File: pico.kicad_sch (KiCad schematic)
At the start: 90 parts, among them J101 Programming, J102 ???, J103 XT60, J104 MR30, J105 MR30, Q101 IRFS7434TRL7PP, Q102 SQJ142EP-T1_GE3, Q103 SQJ142EP-T1_GE3, Q104 SQJ142EP-T1_GE3, Q105 SQJ142EP-T1_GE3, Q106 SQJ142EP-T1_GE3, Q107 SQJ142EP-T1_GE3, Q108 SQJ142EP-T1_GE3, Q109 SQJ142EP-T1_GE3, Q110 SQJ142EP-T1_GE3, Q111 SQJ142EP-T1_GE3, Q112 SQJ142EP-T1_GE3, Q113 SQJ142EP-T1_GE3, U101 TPS7A2050PDBVR, U104 DRV8323SRTAT, U105 DRV8323SRTAT, U106 ADC124S051CIMM/NOPB

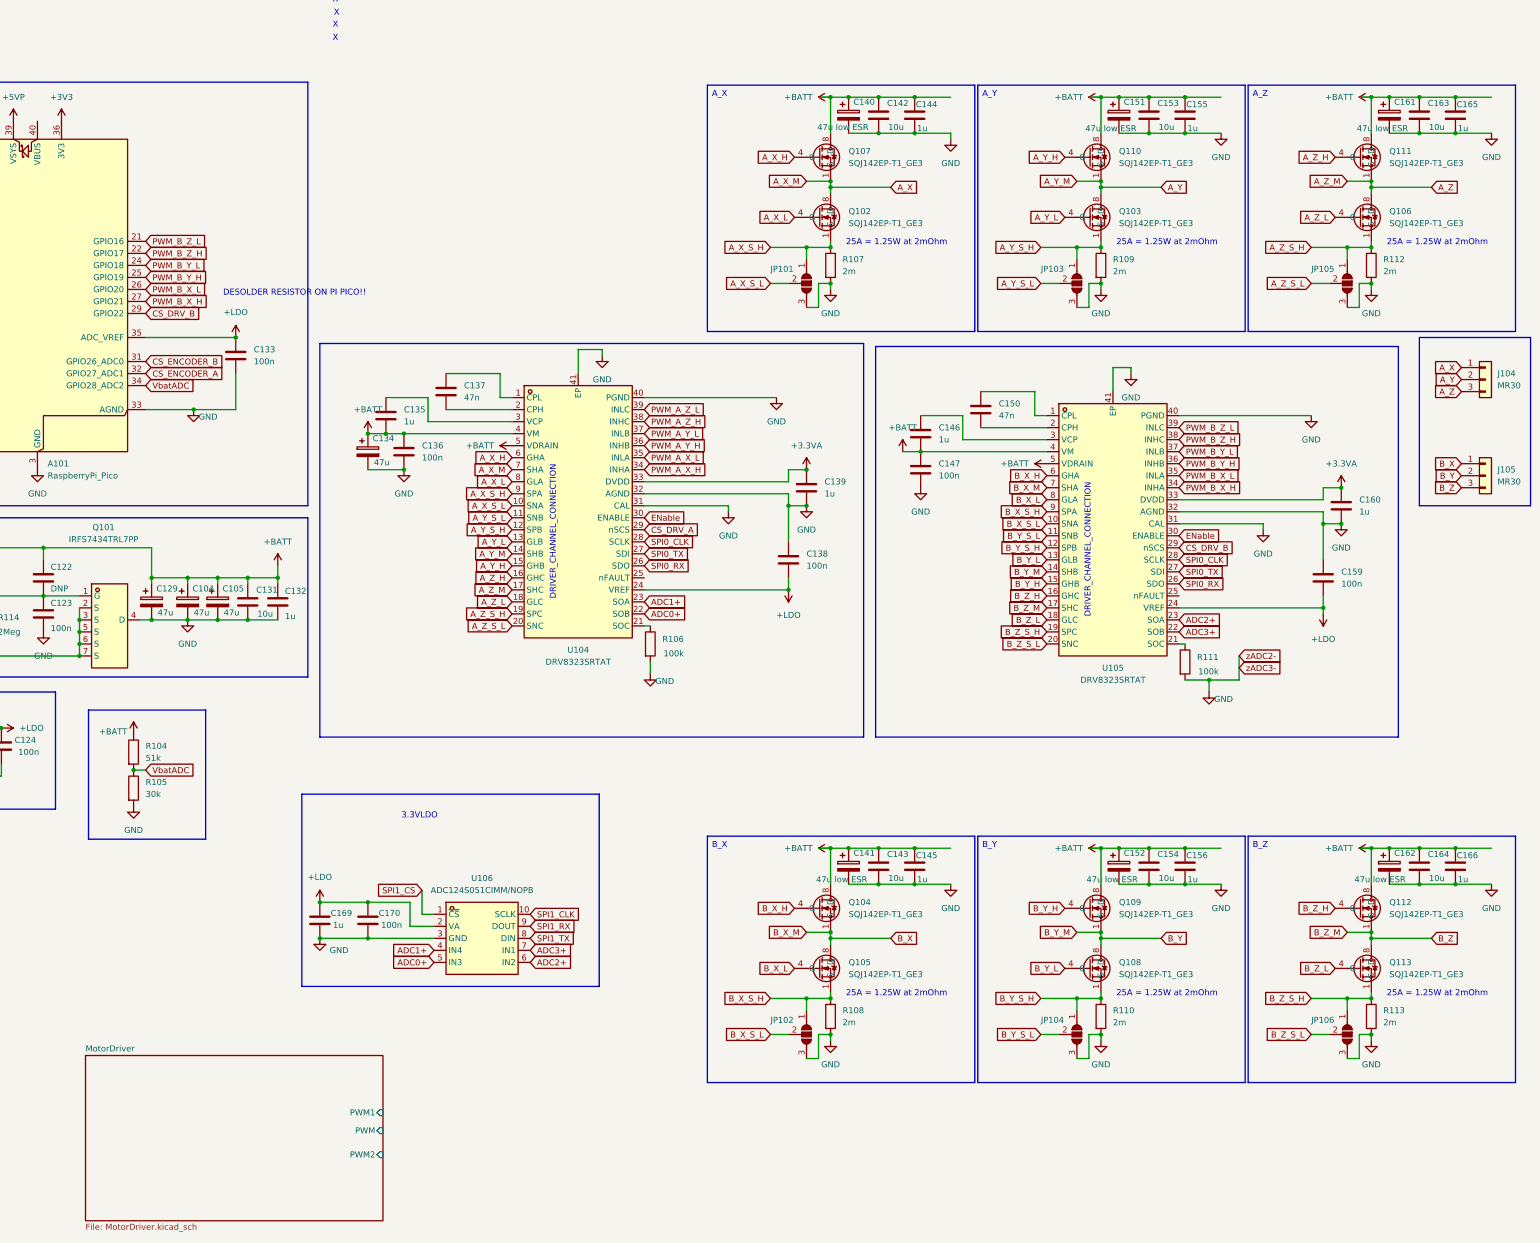
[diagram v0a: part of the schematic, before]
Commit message: seprate motors
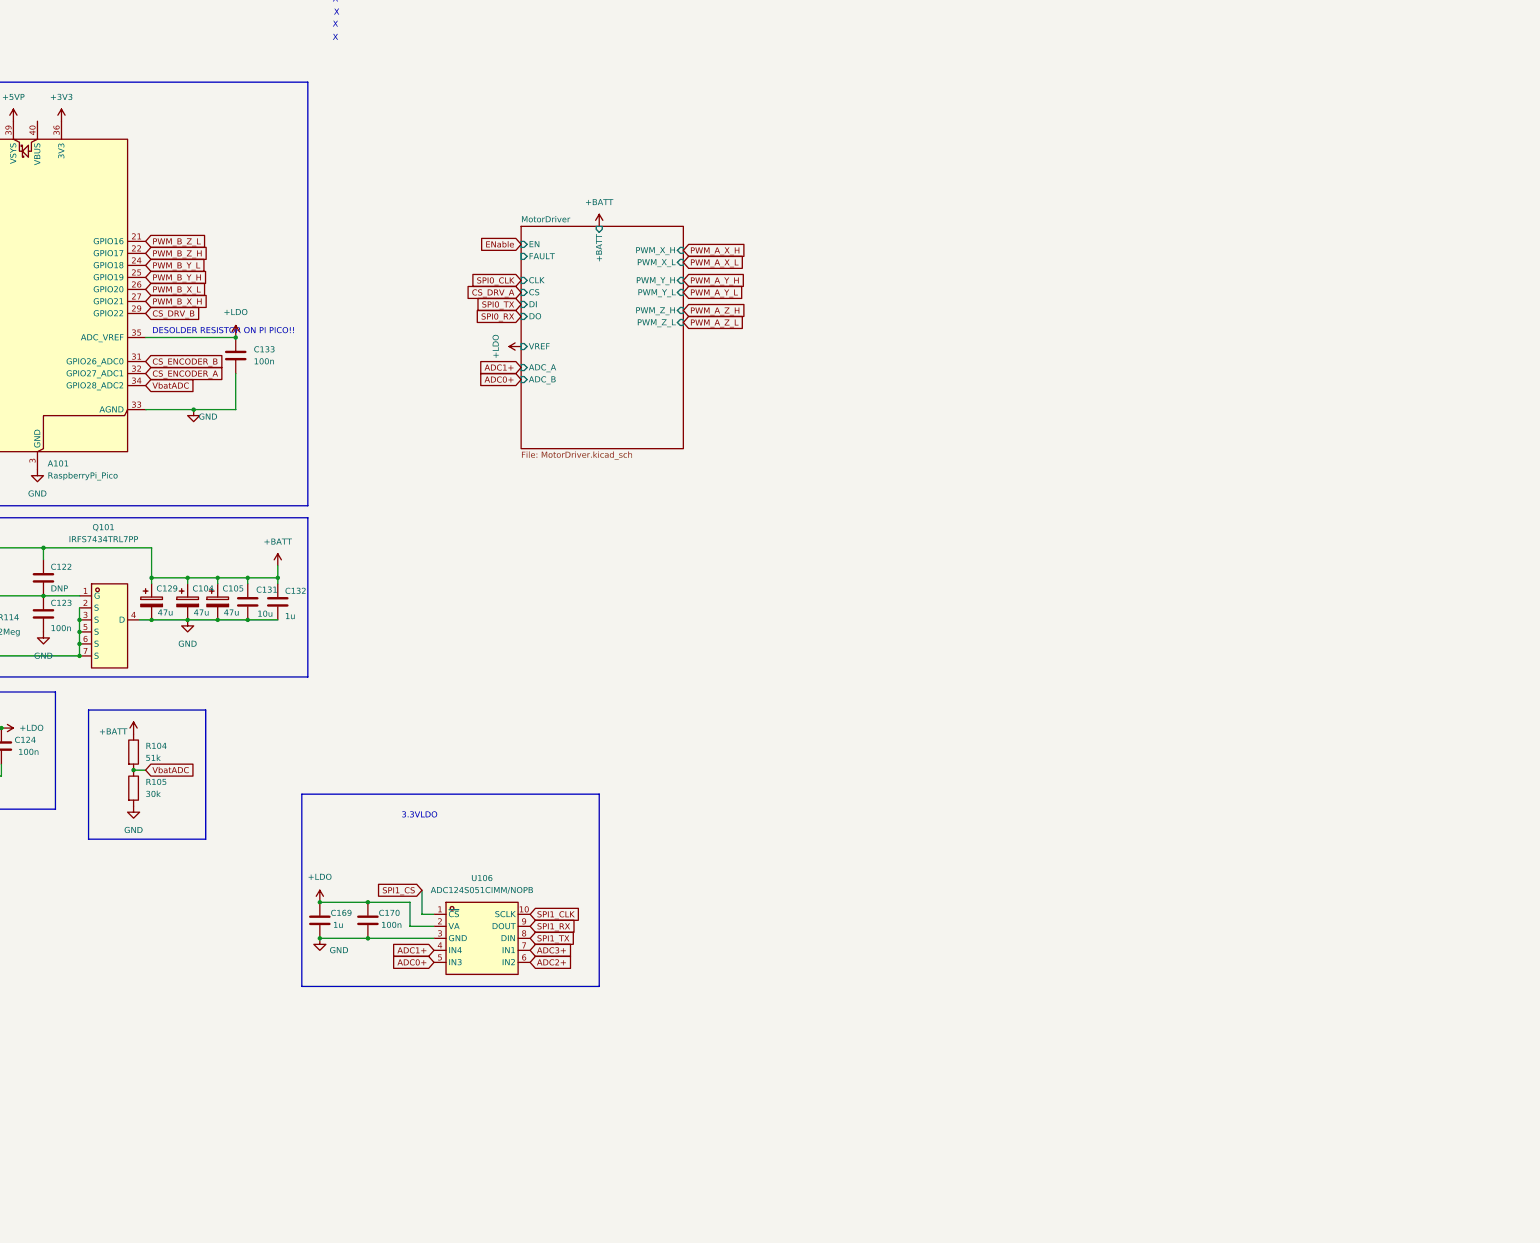
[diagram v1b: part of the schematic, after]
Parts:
- removed C134: 47u, Capacitor_THT:CP_Radial_D6.3mm_P2.50mm, symbol Device:C_Polarized
- removed C135, C139, C144, C145, C146, C155, C156, C160, C165, C166: 1u, COMPONENTS:1206_Resistor, symbol Device:C
- removed C136, C138, C147, C159: 100n, COMPONENTS:1206_Resistor, symbol Device:C
- removed C137, C150: 47n, COMPONENTS:1206_Resistor, symbol Device:C
- removed C140, C141, C151, C152, C161, C162: 47u low ESR, Capacitor_THT:CP_Radial_D6.3mm_P2.50mm, symbol Device:C_Polarized
- removed C142, C143, C153, C154, C163, C164: 10u, COMPONENTS:1206_Resistor, symbol Device:C
- removed J104, J105: MR30, Connector_AMASS:AMASS_MR30PW-FB_1x03_P3.50mm_Horizontal, symbol Connector_Generic:Conn_01x03
- removed JP101, JP102, JP103, JP104, JP105, JP106: SolderJumper_3_Open, Jumper:SolderJumper-3_P1.3mm_Open_RoundedPad1.0x1.5mm_NumberLabels, symbol Jumper:SolderJumper_3_Open
- removed Q102, Q103, Q104, Q105, Q106, Q107, Q108, Q109, Q110, Q111, Q112, Q113: SQJ142EP-T1_GE3, JLCPCB_Transistors_Thyristors:POWERPAK-SO-8_L5.9-W4.9-P1.27-BL, symbol JLCPCB_Transistors_Thyristors:SQJ142EP-T1_GE3
- removed R106, R111: 100k, COMPONENTS:1206_Resistor, symbol Device:R
- removed R107, R108, R109, R110, R112, R113: 2m, COMPONENTS:1206_Resistor, symbol Device:R
- removed U104, U105: DRV8323SRTAT, JLCPCB_Power_Supply_Chip:WQFN-40_L6.0-W6.0-P0.50-TL-EP4.5, symbol JLCPCB_Power_Supply_Chip:DRV8323SRTAT
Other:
- sheet MotorDriver ports: added +BATT, ADC_A, ADC_B, CLK, CS, DI, DO, EN, FAULT, PWM_X_H, PWM_X_L, PWM_Y_H, PWM_Y_L, PWM_Z_H, PWM_Z_L, VREF; removed PWM, PWM1, PWM2
- note removed: "25A = 1.25W at 2mOhm"
- note removed: "DRIVER_CHANNEL_CONNECTION"

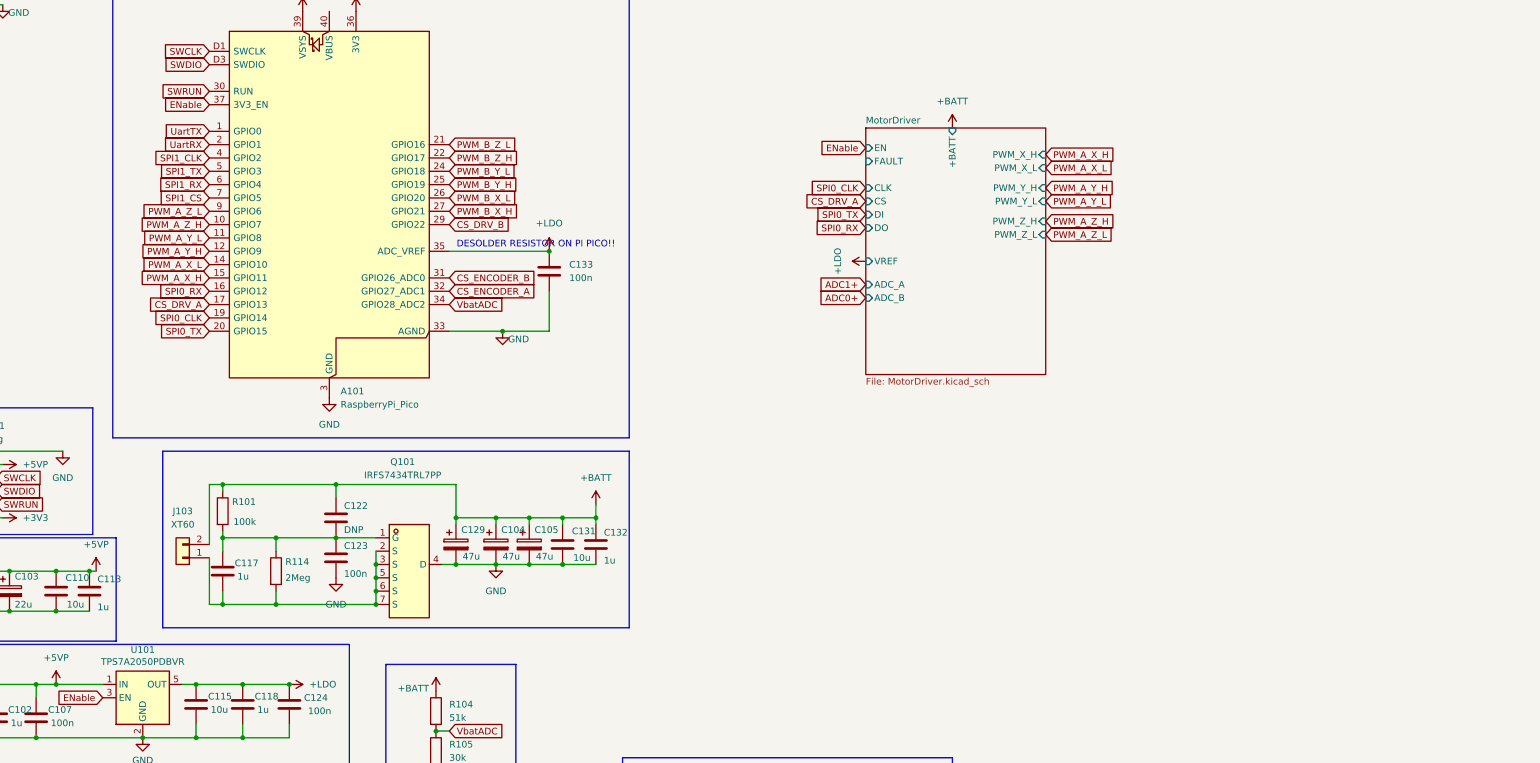
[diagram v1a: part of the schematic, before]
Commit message: progress on pcb todo:encoders
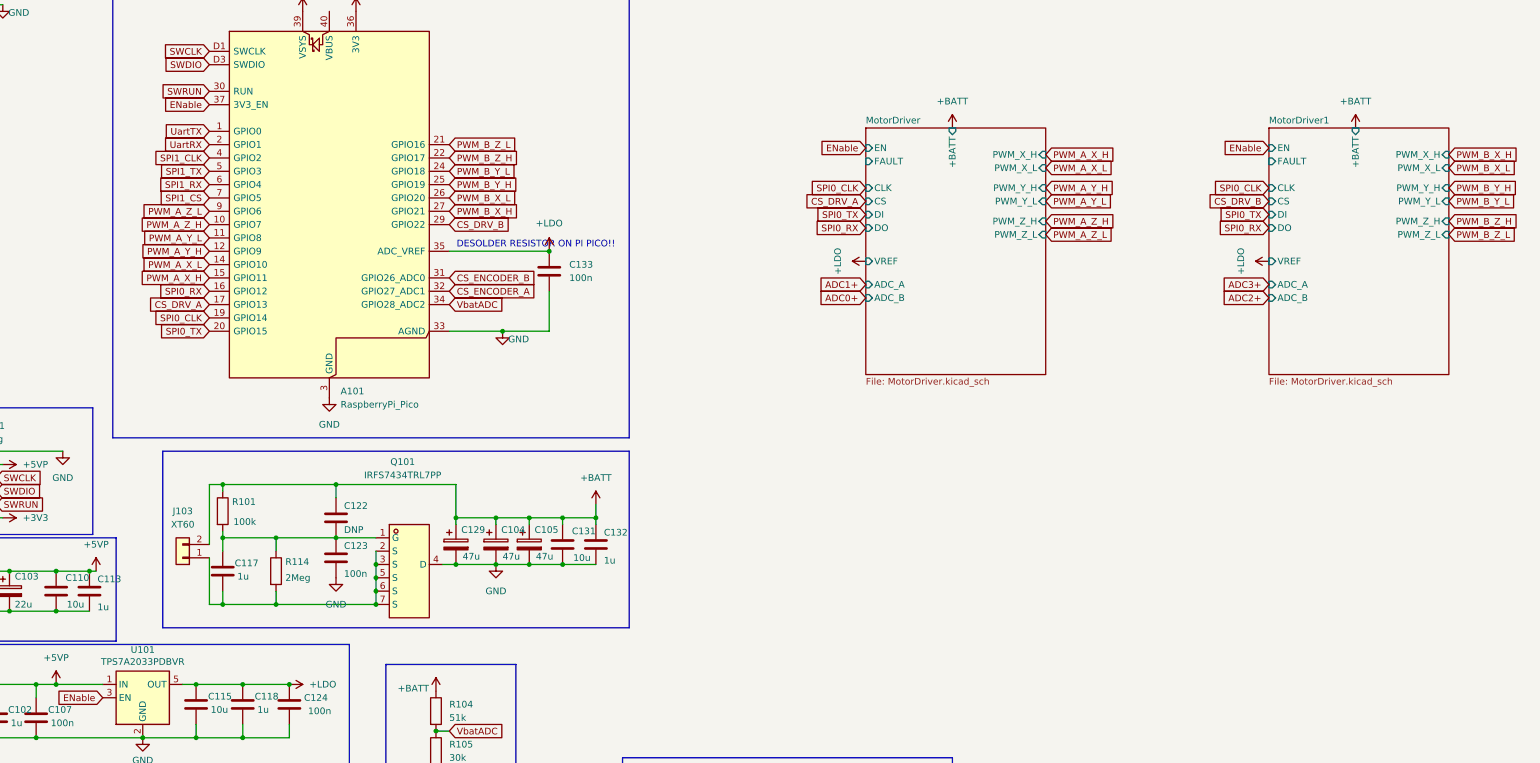
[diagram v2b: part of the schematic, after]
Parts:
- U101: value TPS7A2050PDBVR -> TPS7A2033PDBVR
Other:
- added sheet MotorDriver1 (MotorDriver.kicad_sch)

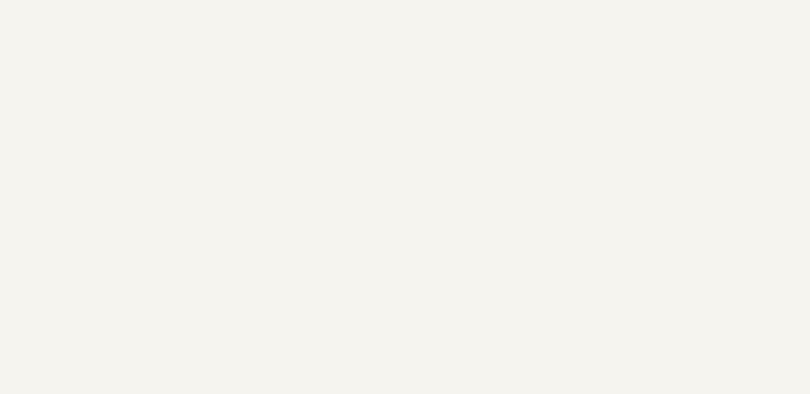
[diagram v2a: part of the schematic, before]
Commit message: added m3 mounting holes
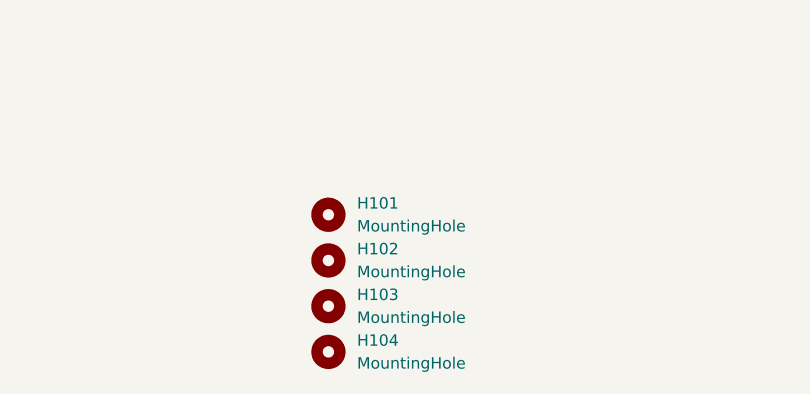
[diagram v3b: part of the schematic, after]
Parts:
- added H101, H102, H103, H104: MountingHole, MountingHole:MountingHole_3.2mm_M3, symbol Mechanical:MountingHole

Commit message: ewdwad
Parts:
- added J104: Conn_01x03, Connector_JST:JST_EH_B3B-EH-A_1x03_P2.50mm_Vertical, symbol Connector_Generic:Conn_01x03
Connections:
- net ENable: now also J104.1 (Pin_1)
- net UartRX: now also J104.2 (Pin_2)
- net UartTX: now also J104.3 (Pin_3)
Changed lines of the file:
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@@
 		)
 	)
+	(global_label "UartRX"
+		(shape input)
+		(at 31.75 66.04 0)
+		(fields_autoplaced yes)
+		(effects
+			(font
+				(size 1.27 1.27)
+			)
+			(justify left)
+		)
+		(property "Intersheetrefs" "${INTERSHEET_REFS}"
+			(at 41.2061 66.04 0)
+			(effects
+				(font
+					(size 1.27 1.27)
+				)
+				(justify left)
+				(hide yes)
+			)
+		)
+	)
 	(global_label "ADC1+"
 		(shape input)
@@
 		)
 	)
+	(global_label "ENable"
+		(shape input)
+		(at 31.75 68.58 0)
+		(fields_autoplaced yes)
+		(effects
+			(font
+				(size 1.27 1.27)
+			)
+			(justify left)
+		)
+		(property "Intersheetrefs" "${INTERSHEET_REFS}"
+			(at 41.2665 68.58 0)
+			(effects
+				(font
+					(size 1.27 1.27)
+				)
+				(justify left)
+				(hide yes)
+			)
+		)
+	)
+	(global_label "UartTX"
+		(shape input)
+		(at 31.75 63.5 0)
+		(fields_autoplaced yes)
+		(effects
+			(font
+				(size 1.27 1.27)
+			)
+			(justify left)
+		)
+		(property "Intersheetrefs" "${INTERSHEET_REFS}"
+			(at 40.9037 63.5 0)
+			(effects
+				(font
+					(size 1.27 1.27)
+				)
+				(justify left)
+				(hide yes)
+			)
+		)
+	)
 	(global_label "SPI1_CS"
 		(shape input)
@@
 					(unit 1)
 				)
+			)
+		)
+	)
+	(symbol
+		(lib_id "Connector_Generic:Conn_01x03")
+		(at 26.67 66.04 180)
+		(unit 1)
+		(exclude_from_sim no)
+		(in_bom yes)
+		(on_board yes)
+		(dnp no)
+		(fields_autoplaced yes)
+		(property "Reference" "J104"
+			(at 26.67 57.15 0)
+			(effects
+				(font
+					(size 1.27 1.27)
+				)
+			)
+		)
+		(property "Value" "Conn_01x03"
+			(at 26.67 59.69 0)
+			(effects
+				(font
+					(size 1.27 1.27)
+				)
+			)
+		)
+		(property "Footprint" "Connector_JST:JST_EH_B3B-EH-A_1x03_P2.50mm_Vertical"
+			(at 26.67 66.04 0)
+			(effects
+				(font
+					(size 1.27 1.27)
+				)
+				(hide yes)
+			)
+		)
+		(property "Datasheet" "~"
+			(at 26.67 66.04 0)
+			(effects
+				(font
+					(size 1.27 1.27)
+				)
+				(hide yes)
+			)
+		)
+		(property "Description" "Generic connector, single row, 01x03, script generated (kicad-library-utils/schlib/autogen/connector/)"
+			(at 26.67 66.04 0)
+			(effects
+				(font
+					(size 1.27 1.27)
+				)
+				(hide yes)
+			)
+		)
+		(pin "1"
+		)
+		(pin "3"
+		)
+		(pin "2"
+		)
+		(instances
+			(project ""
+				(path "/ee499c9f-2c44-4eb0-b36d-4920617b3177"
+					(reference "J104")
+					(unit 1)
+				)

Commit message: wdawdawd
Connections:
- net ADC2+: now also U106.7 (IN1); no longer U106.6 (IN2)
- net ADC3+: now also U106.6 (IN2); no longer U106.7 (IN1)

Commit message: why every commit needs a message
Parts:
- added Q102: BSS138, Package_TO_SOT_SMD:SOT-23, symbol Transistor_FET:BSS138
- added R102: 100, COMPONENTS:1206_Resistor, symbol Device:R
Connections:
- net +BATT: now also Q102.3 (D)
- net GND: now also R102.2
- net at C117.1, C122.2, C123.1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: now also Q102.2 (S)
- net at C117.2, J103.1 (Pin_1), Q101.2 (S)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: now also R102.1
- new net ENableBATT: Q102.1 (G)
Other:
- note added: "WILL SPLIT GND WORK??"
- moved on the sheet: C101, C102, C107, C115, C118, C124, R104, R105, U101

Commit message: Good progress
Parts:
- removed C117: 1u, COMPONENTS:1206_Resistor, symbol Device:C
- removed C122: DNP, COMPONENTS:1206_Resistor, symbol Device:C
- removed C123: 100n, COMPONENTS:1206_Resistor, symbol Device:C
- removed Q101: IRFS7434TRL7PP, JLCPCB_Transistors:D2PAK-7_L10.6-W9.6-P1.27-LS15.9-BR, symbol JLCPCB_Transistors:IRFS7434TRL7PP
- removed R114: 2Meg, COMPONENTS:1206_Resistor, symbol Device:R
- added C106: 2200u, Capacitor_THT:CP_Radial_D18.0mm_P7.50mm, symbol Device:C_Polarized
- added Q101, Q103, Q104, Q105, Q106: AGM30P100D, EasyEDA_Lib:TO-252-3_L6.6-W6.1-P4.57-LS9.9-BR-CW, symbol EasyEDA_Lib:AGM30P100D
- added R103, R106, R107: 100, COMPONENTS:1206_Resistor, symbol Device:R
- added R108: 5k, COMPONENTS:1206_Resistor, symbol Device:R
- R101: value 100k -> 100
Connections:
- net ENableBATT is gone; now on net ENable: Q102.1 (G)
- net +BATT: now also R101.2, R102.2, C106.1, Q101.2 (D), Q103.2 (D), Q104.2 (D), Q105.2 (D), Q106.2 (D), R103.2, R106.2, R107.2; no longer J103.2 (Pin_2), Q102.3 (D), R101.1
- net GND: now also J103.1 (Pin_1), Q102.2 (S), C106.2; no longer R102.2
- net IN: now reaches R102.1
- net IN: now also J103.2 (Pin_2), R101.1, Q101.3 (S), Q103.3 (S), Q104.3 (S), Q105.3 (S), Q106.3 (S), R103.1, R106.1, R107.1, R108.1; no longer J103.1 (Pin_1)
- new net: Q101.1 (G), Q102.3 (D), Q103.1 (G), Q104.1 (G), Q105.1 (G), Q106.1 (G), R108.2
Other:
- note removed: "WILL SPLIT GND WORK??"
- moved on the sheet: C101, C102, C103, C104, C105, C107, C110, C113, C115, C118, C124, C129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

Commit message: done?
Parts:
- removed C103: 22u, Capacitor_THT:CP_Radial_D5.0mm_P2.00mm, symbol Device:C_Polarized
- removed C131: 10u, COMPONENTS:1206_Resistor, symbol Device:C
- removed C132: 1u, COMPONENTS:1206_Resistor, symbol Device:C
- removed H101, H102, H103, H104: MountingHole, MountingHole:MountingHole_3.2mm_M3, symbol Mechanical:MountingHole
- removed J101: Programming, Connector_PinHeader_2.54mm:PinHeader_1x06_P2.54mm_Vertical, symbol Connector:Conn_01x06_Socket
- removed J102: ???, Connector_PinHeader_2.54mm:PinHeader_1x02_P2.54mm_Vertical, symbol Connector_Generic:Conn_01x02
- added H105, H106, H107, H108: MountingHole_Pad, MountingHole:MountingHole_3.2mm_M3_Pad_Via, symbol Mechanical:MountingHole_Pad
- added J101, J105, J106, J107, J108: Conn_01x03, Connector_JST:JST_XH_B3B-XH-A_1x03_P2.50mm_Vertical, symbol Connector_Generic:Conn_01x03
- added JP101: SolderJumper_2_Open, Jumper:SolderJumper-2_P1.3mm_Open_RoundedPad1.0x1.5mm, symbol Jumper:SolderJumper_2_Open
- J104: footprint Connector_JST:JST_EH_B3B-EH-A_1x03_P2.50mm_Vertical -> Connector_JST:JST_XH_B3B-XH-A_1x03_P2.50mm_Vertical
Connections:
- net +5VP: now also J101.3 (Pin_3)
- net +LDO: now also J105.2 (Pin_2), J107.2 (Pin_2)
- net CS_ENCODER_A: now also J105.1 (Pin_1)
- net CS_ENCODER_B: now also J107.1 (Pin_1)
- net ENable: now also JP101.1 (A); no longer A101.37 (3V3_EN)
- net GND: now also H105.1, H106.1, H107.1, H108.1, J101.1 (Pin_1), J105.3 (Pin_3), J107.3 (Pin_3)
- net SPI0_CLK: now also J106.3 (Pin_3), J108.3 (Pin_3)
- net SPI0_RX: now also J106.1 (Pin_1), J108.1 (Pin_1)
- net SPI0_TX: now also J106.2 (Pin_2), J108.2 (Pin_2)
- new net: A101.37 (3V3_EN), JP101.2 (B)
